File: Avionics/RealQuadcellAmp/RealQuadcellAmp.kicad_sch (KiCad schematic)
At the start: 45 parts, among them U1 OPA1642AID, U2 OPA1642AID, U3 OPA1642AID, U4 OPA1642AID

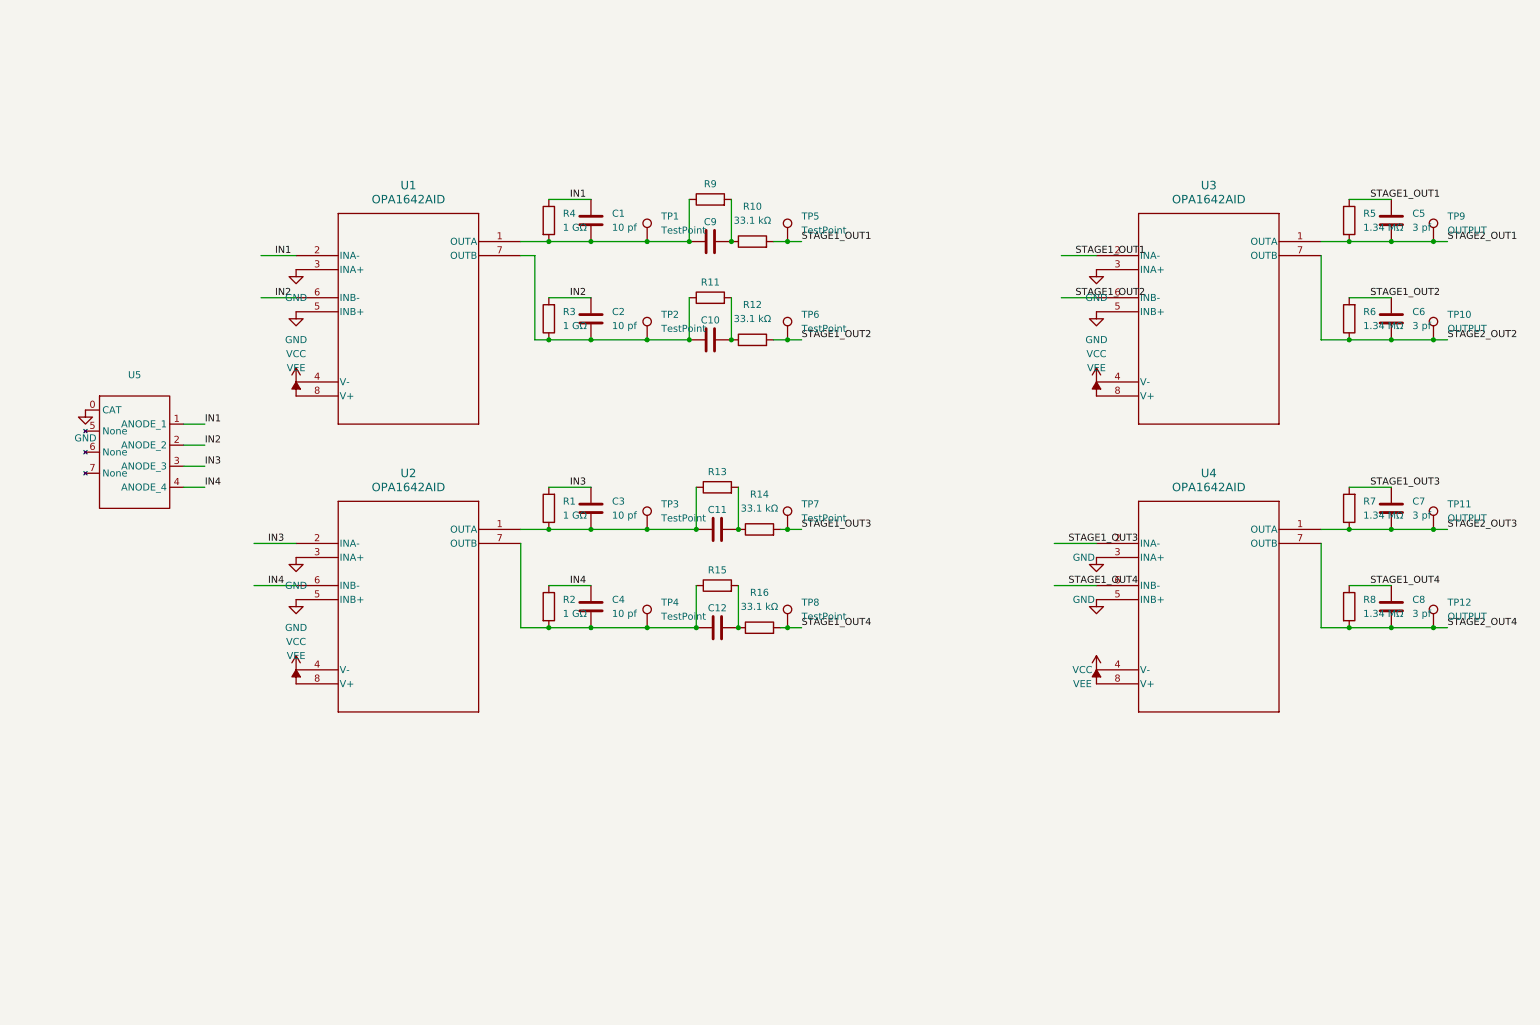
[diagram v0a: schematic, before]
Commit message: added voltage divider and adjusted routing of quadcell
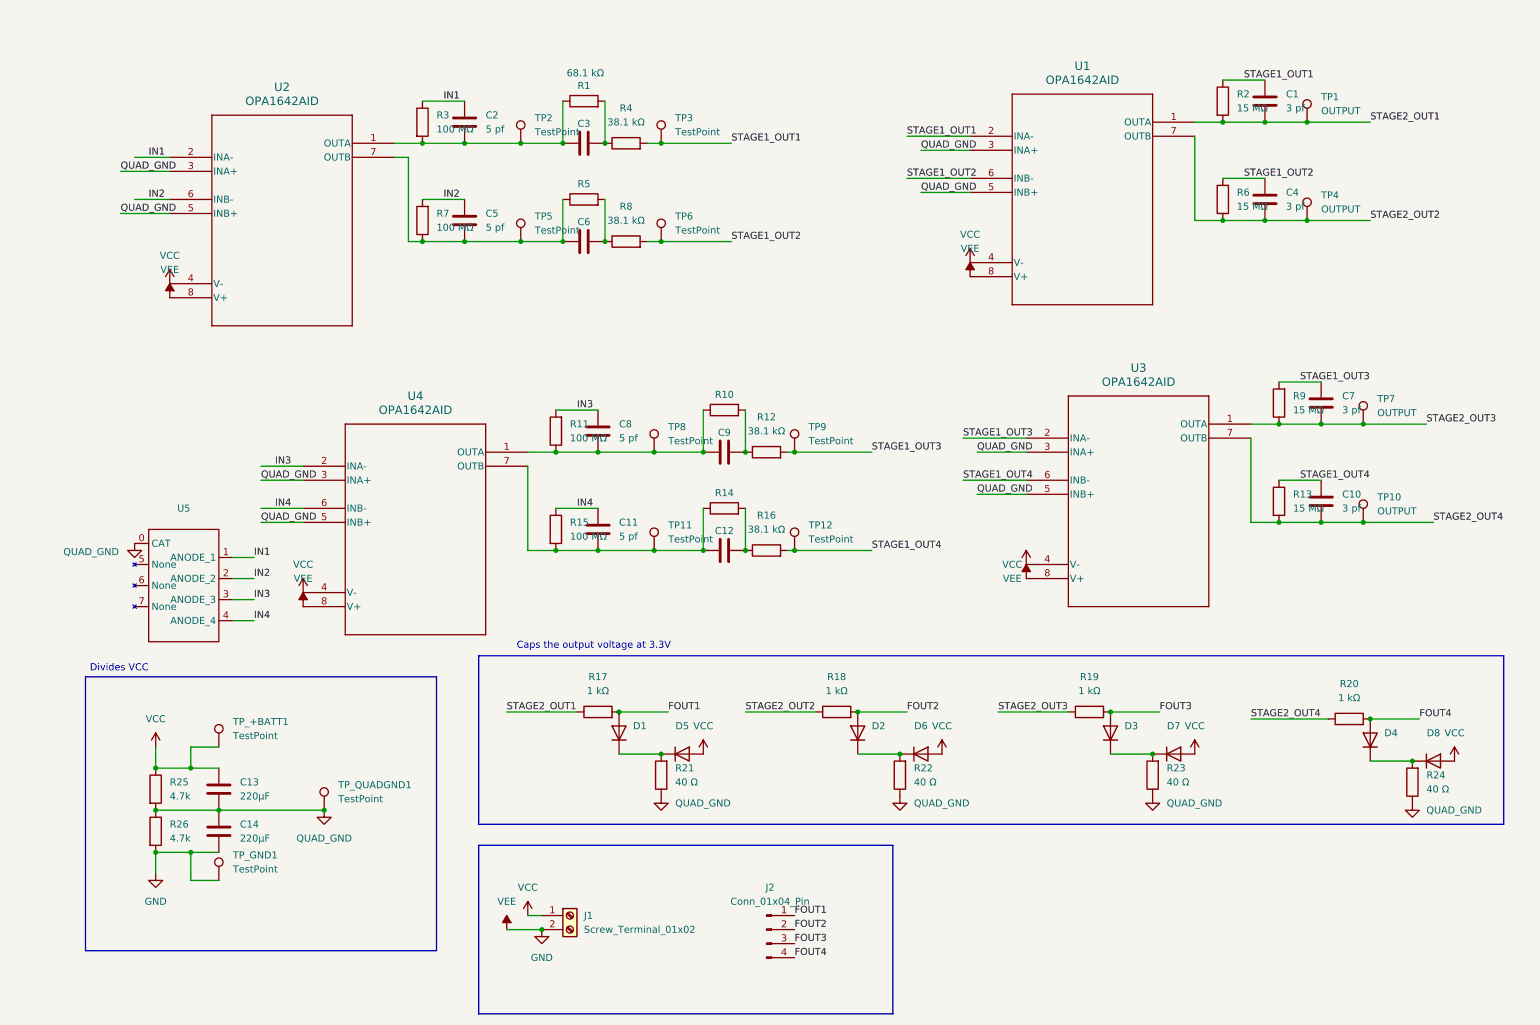
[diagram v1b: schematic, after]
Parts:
- added C13, C14: 220µF, Capacitor_SMD:C_0805_2012Metric_Pad1.18x1.45mm_HandSolder, symbol Device:C
- added D1, D2, D3, D4, D5, D6, D7, D8: ~, Diode_SMD:D_0805_2012Metric_Pad1.15x1.40mm_HandSolder, symbol Diode:1N4001
- added J1: Screw_Terminal_01x02, TerminalBlock:TerminalBlock_bornier-2_P5.08mm, symbol Connector:Screw_Terminal_01x02
- added J2: Conn_01x04_Pin, Connector_PinHeader_2.54mm:PinHeader_1x04_P2.54mm_Vertical, symbol Connector:Conn_01x04_Pin
- added R17, R18, R19, R20: 1 kΩ, Resistor_SMD:R_0805_2012Metric_Pad1.20x1.40mm_HandSolder, symbol Device:R
- added R21, R22, R23, R24: 40 Ω, Resistor_SMD:R_0805_2012Metric_Pad1.20x1.40mm_HandSolder, symbol Device:R
- added R25, R26: 4.7k, Resistor_SMD:R_0805_2012Metric_Pad1.20x1.40mm_HandSolder, symbol Device:R
- added TP_+BATT1, TP_GND1, TP_QUADGND1: TestPoint, TestPoint:TestPoint_THTPad_1.0x1.0mm_Drill0.5mm, symbol Connector:TestPoint
- C1: renamed from C5; footprint Capacitor_SMD:C_0603_1608Metric_Pad1.08x0.95mm_HandSolder -> Capacitor_SMD:C_0805_2012Metric_Pad1.18x1.45mm_HandSolder
- C10: renamed from C8; footprint Capacitor_SMD:C_0603_1608Metric_Pad1.08x0.95mm_HandSolder -> Capacitor_SMD:C_0805_2012Metric_Pad1.18x1.45mm_HandSolder
- C11: renamed from C4; value 10 pf -> 5 pf; footprint Capacitor_SMD:C_0603_1608Metric_Pad1.08x0.95mm_HandSolder -> Capacitor_SMD:C_0805_2012Metric_Pad1.18x1.45mm_HandSolder
- C12, C7: footprint Capacitor_SMD:C_0603_1608Metric_Pad1.08x0.95mm_HandSolder -> Capacitor_SMD:C_0805_2012Metric_Pad1.18x1.45mm_HandSolder
- C2: renamed from C1; value 10 pf -> 5 pf; footprint Capacitor_SMD:C_0603_1608Metric_Pad1.08x0.95mm_HandSolder -> Capacitor_SMD:C_0805_2012Metric_Pad1.18x1.45mm_HandSolder
- C3: renamed from C9; footprint Capacitor_SMD:C_0603_1608Metric_Pad1.08x0.95mm_HandSolder -> Capacitor_SMD:C_0805_2012Metric_Pad1.18x1.45mm_HandSolder
- C4: renamed from C6; footprint Capacitor_SMD:C_0603_1608Metric_Pad1.08x0.95mm_HandSolder -> Capacitor_SMD:C_0805_2012Metric_Pad1.18x1.45mm_HandSolder
- C5: renamed from C2; value 10 pf -> 5 pf; footprint Capacitor_SMD:C_0603_1608Metric_Pad1.08x0.95mm_HandSolder -> Capacitor_SMD:C_0805_2012Metric_Pad1.18x1.45mm_HandSolder
- C6: renamed from C10; footprint Capacitor_SMD:C_0603_1608Metric_Pad1.08x0.95mm_HandSolder -> Capacitor_SMD:C_0805_2012Metric_Pad1.18x1.45mm_HandSolder
- C8: renamed from C3; value 10 pf -> 5 pf; footprint Capacitor_SMD:C_0603_1608Metric_Pad1.08x0.95mm_HandSolder -> Capacitor_SMD:C_0805_2012Metric_Pad1.18x1.45mm_HandSolder
- C9: renamed from C11; footprint Capacitor_SMD:C_0603_1608Metric_Pad1.08x0.95mm_HandSolder -> Capacitor_SMD:C_0805_2012Metric_Pad1.18x1.45mm_HandSolder
- R1: renamed from R9; value 0.1 MΩ -> 68.1 kΩ; footprint Resistor_SMD:R_0603_1608Metric_Pad0.98x0.95mm_HandSolder -> Resistor_SMD:R_0805_2012Metric_Pad1.20x1.40mm_HandSolder
- R10: renamed from R13; value 0.1 MΩ -> 68.1 kΩ; footprint Resistor_SMD:R_0603_1608Metric_Pad0.98x0.95mm_HandSolder -> Resistor_SMD:R_0805_2012Metric_Pad1.20x1.40mm_HandSolder
- R11: renamed from R1; value 1 GΩ -> 100 MΩ; footprint Resistor_SMD:R_1206_3216Metric_Pad1.30x1.75mm_HandSolder -> Resistor_SMD:R_0805_2012Metric_Pad1.20x1.40mm_HandSolder
- R12: renamed from R14; value 33.1 kΩ -> 38.1 kΩ; footprint Resistor_SMD:R_0603_1608Metric_Pad0.98x0.95mm_HandSolder -> Resistor_SMD:R_0805_2012Metric_Pad1.20x1.40mm_HandSolder
- R13: renamed from R8; value 1.34 MΩ -> 15 MΩ; footprint Resistor_SMD:R_0603_1608Metric_Pad0.98x0.95mm_HandSolder -> Resistor_SMD:R_0805_2012Metric_Pad1.20x1.40mm_HandSolder
- R14: renamed from R15; value 0.1 MΩ -> 68.1 kΩ; footprint Resistor_SMD:R_0603_1608Metric_Pad0.98x0.95mm_HandSolder -> Resistor_SMD:R_0805_2012Metric_Pad1.20x1.40mm_HandSolder
- R15: renamed from R2; value 1 GΩ -> 100 MΩ; footprint Resistor_SMD:R_1206_3216Metric_Pad1.30x1.75mm_HandSolder -> Resistor_SMD:R_0805_2012Metric_Pad1.20x1.40mm_HandSolder
- R16: value 33.1 kΩ -> 38.1 kΩ; footprint Resistor_SMD:R_0603_1608Metric_Pad0.98x0.95mm_HandSolder -> Resistor_SMD:R_0805_2012Metric_Pad1.20x1.40mm_HandSolder
- R2: renamed from R5; value 1.34 MΩ -> 15 MΩ; footprint Resistor_SMD:R_0603_1608Metric_Pad0.98x0.95mm_HandSolder -> Resistor_SMD:R_0805_2012Metric_Pad1.20x1.40mm_HandSolder
- R3: renamed from R4; value 1 GΩ -> 100 MΩ; footprint Resistor_SMD:R_1206_3216Metric_Pad1.30x1.75mm_HandSolder -> Resistor_SMD:R_0805_2012Metric_Pad1.20x1.40mm_HandSolder
- R4: renamed from R10; value 33.1 kΩ -> 38.1 kΩ; footprint Resistor_SMD:R_0603_1608Metric_Pad0.98x0.95mm_HandSolder -> Resistor_SMD:R_0805_2012Metric_Pad1.20x1.40mm_HandSolder
- R5: renamed from R11; value 0.1 MΩ -> 68.1 kΩ; footprint Resistor_SMD:R_0603_1608Metric_Pad0.98x0.95mm_HandSolder -> Resistor_SMD:R_0805_2012Metric_Pad1.20x1.40mm_HandSolder
- R6: value 1.34 MΩ -> 15 MΩ; footprint Resistor_SMD:R_0603_1608Metric_Pad0.98x0.95mm_HandSolder -> Resistor_SMD:R_0805_2012Metric_Pad1.20x1.40mm_HandSolder
- R7: renamed from R3; value 1 GΩ -> 100 MΩ; footprint Resistor_SMD:R_1206_3216Metric_Pad1.30x1.75mm_HandSolder -> Resistor_SMD:R_0805_2012Metric_Pad1.20x1.40mm_HandSolder
- R8: renamed from R12; value 33.1 kΩ -> 38.1 kΩ; footprint Resistor_SMD:R_0603_1608Metric_Pad0.98x0.95mm_HandSolder -> Resistor_SMD:R_0805_2012Metric_Pad1.20x1.40mm_HandSolder
- R9: renamed from R7; value 1.34 MΩ -> 15 MΩ; footprint Resistor_SMD:R_0603_1608Metric_Pad0.98x0.95mm_HandSolder -> Resistor_SMD:R_0805_2012Metric_Pad1.20x1.40mm_HandSolder
- renumbered TP9 to TP1, TP12 to TP10, TP4 to TP11, TP8 to TP12, TP1 to TP2, TP5 to TP3, TP10 to TP4, TP2 to TP5, TP11 to TP7, TP3 to TP8, TP7 to TP9, U3 to U1, U1 to U2, U4 to U3, U2 to U4
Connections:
- net VEE is gone; now on net GND: U1.8 (V+), U2.8 (V+), U3.8 (V+), U4.8 (V+)
- net GND: now also C14.2, J1.2 (Pin_2), R26.2, TP_GND1.1; no longer U1.3 (INA+), U1.5 (INB+), U2.3 (INA+), U2.5 (INB+), U3.3 (INA+), U3.5 (INB+), U4.3 (INA+), U4.5 (INB+), U5.0 (CAT)
- net STAGE2_OUT1: now also R17.1
- net STAGE2_OUT2: now also R18.1
- net STAGE2_OUT3: now also R19.1
- net STAGE2_OUT4: now also R20.1
- net VCC: now also C13.1, D5.2 (A), D6.2 (A), D7.2 (A), D8.2 (A), J1.1 (Pin_1), R25.1, TP_+BATT1.1
- new net: D4.1 (K), D8.1 (K), R24.2
- new net: D1.1 (K), D5.1 (K), R21.2
- new net: D3.1 (K), D7.1 (K), R23.2
- new net: D2.1 (K), D6.1 (K), R22.2
- new net FOUT1: D1.2 (A), J2.1 (Pin_1), R17.2
- new net FOUT2: D2.2 (A), J2.2 (Pin_2), R18.2
- new net FOUT3: D3.2 (A), J2.3 (Pin_3), R19.2
- new net FOUT4: D4.2 (A), J2.4 (Pin_4), R20.2
- new net QUAD_GND: C13.2, C14.1, R21.1, R22.1, R23.1, R24.1, R25.2, R26.1, TP_QUADGND1.1, U1.3 (INA+), U1.5 (INB+), U2.3 (INA+), U2.5 (INB+), U3.3 (INA+), U3.5 (INB+), U4.3 (INA+), U4.5 (INB+), U5.0 (CAT)
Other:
- note added: "Caps the output voltage at 3.3V"
- note added: "Divides VCC"
- moved on the sheet: C1, C10, C11, C12, C2, C3, C4, C5, C6, C7, C8, C9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

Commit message: a few more small tweaks to quadcell
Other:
- moved on the sheet: C11, C12, C8, C9, R10, R11, R12, R14, R15, R16, TP11, TP12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

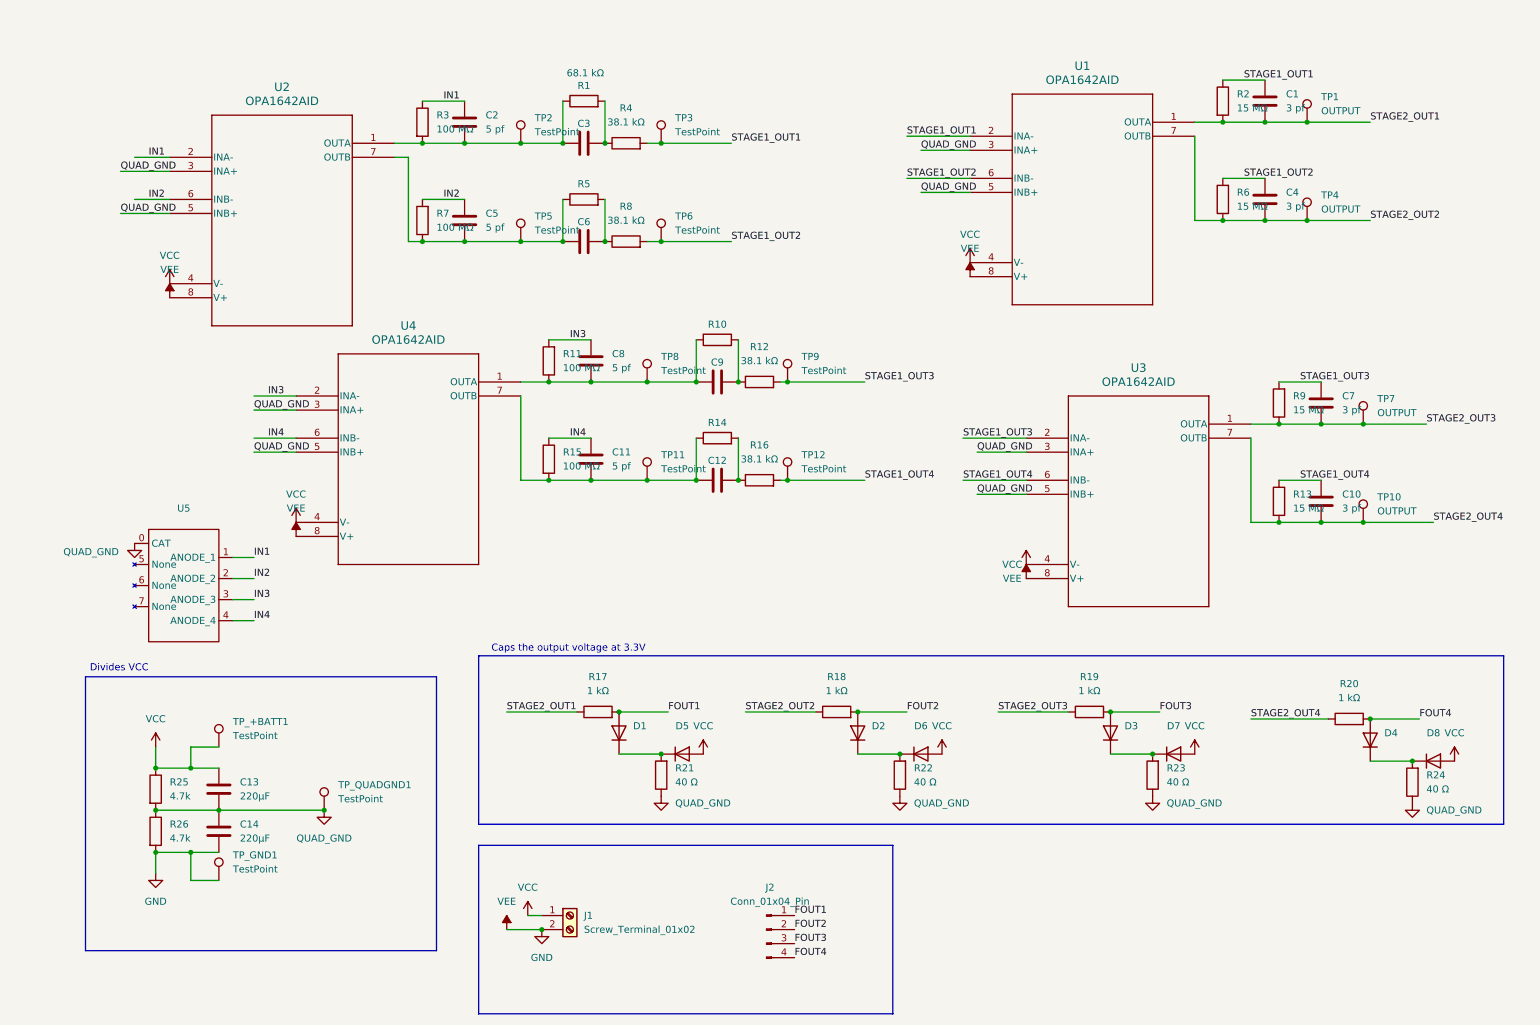
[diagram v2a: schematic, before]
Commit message: added voltage divider to quadcell
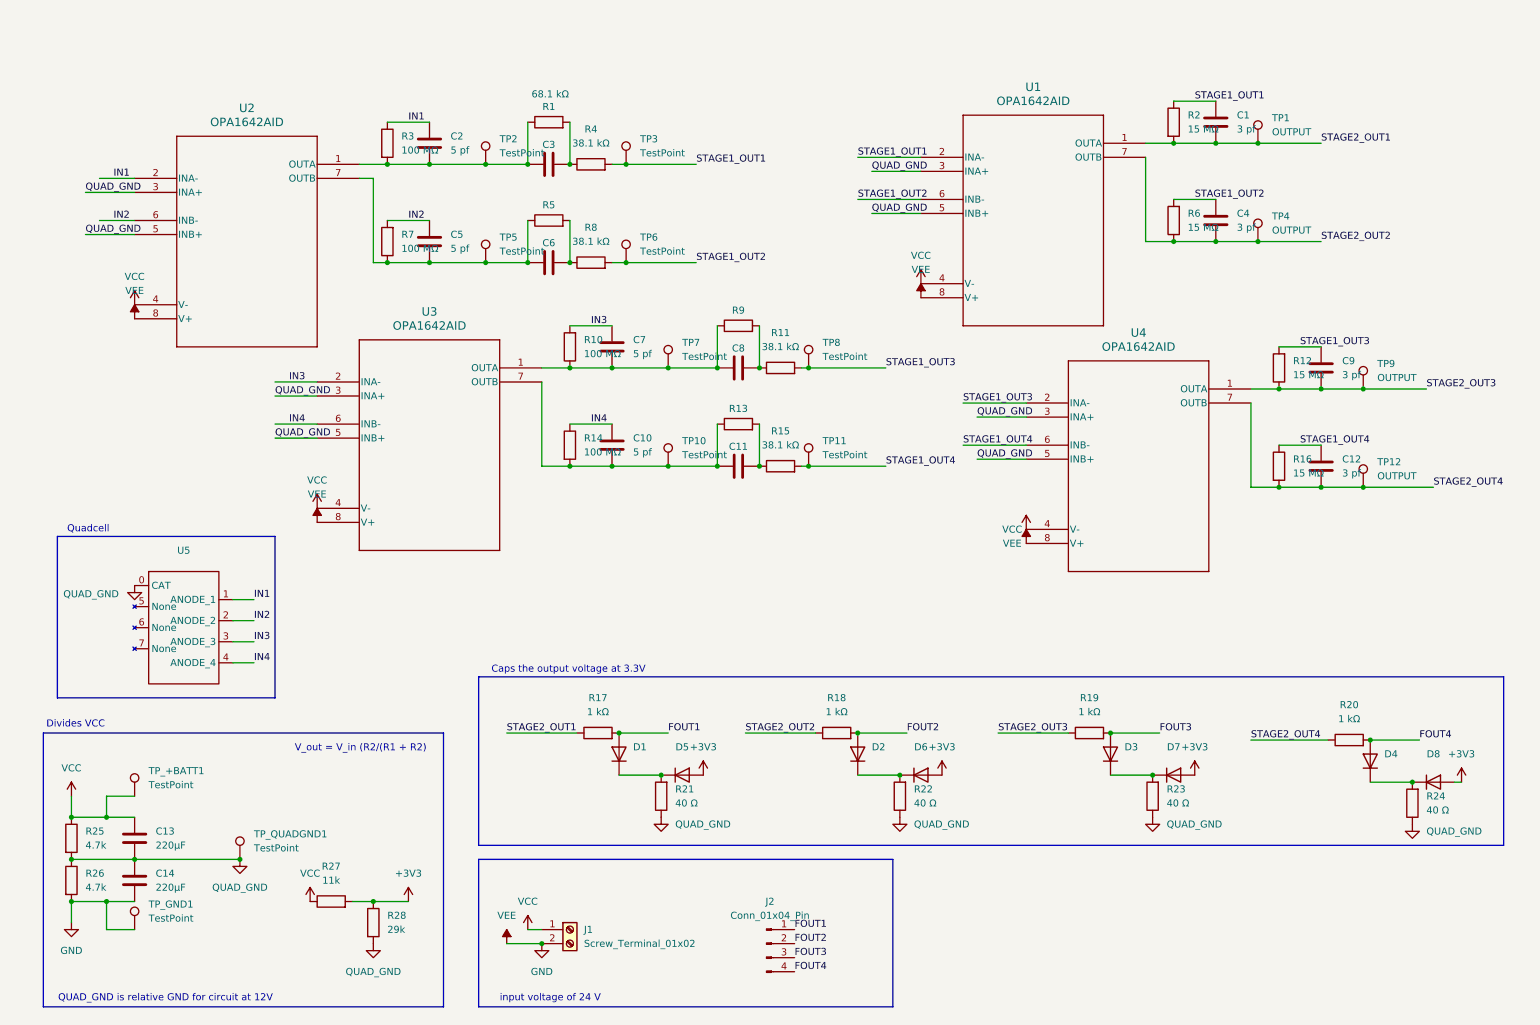
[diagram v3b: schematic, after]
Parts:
- added R27: 11k, Resistor_SMD:R_0805_2012Metric_Pad1.20x1.40mm_HandSolder, symbol Device:R
- added R28: 29k, Resistor_SMD:R_0805_2012Metric_Pad1.20x1.40mm_HandSolder, symbol Device:R
- renumbered C11 to C10, C12 to C11, C10 to C12, C8 to C7, C9 to C8, C7 to C9, R11 to R10, R12 to R11, R9 to R12, R14 to R13, R15 to R14, R16 to R15, R13 to R16, R10 to R9, TP11 to TP10, TP12 to TP11, TP10 to TP12, TP8 to TP7, TP9 to TP8, TP7 to TP9, U4 to U3, U3 to U4
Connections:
- net QUAD_GND: now also R28.2
- net VCC: now also R27.1; no longer D5.2 (A), D6.2 (A), D7.2 (A), D8.2 (A)
- new net +3V3: D5.2 (A), D6.2 (A), D7.2 (A), D8.2 (A), R27.2, R28.1
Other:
- note added: "QUAD_GND is relative GND for circuit at 12V"
- note added: "Quadcell"
- note added: "V_out = V_in (R2/(R1 + R2)"
- note added: "input voltage of 24 V"
- moved on the sheet: C1, C10, C11, C12, C13, C14, C2, C3, C4, C5, C6, C7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

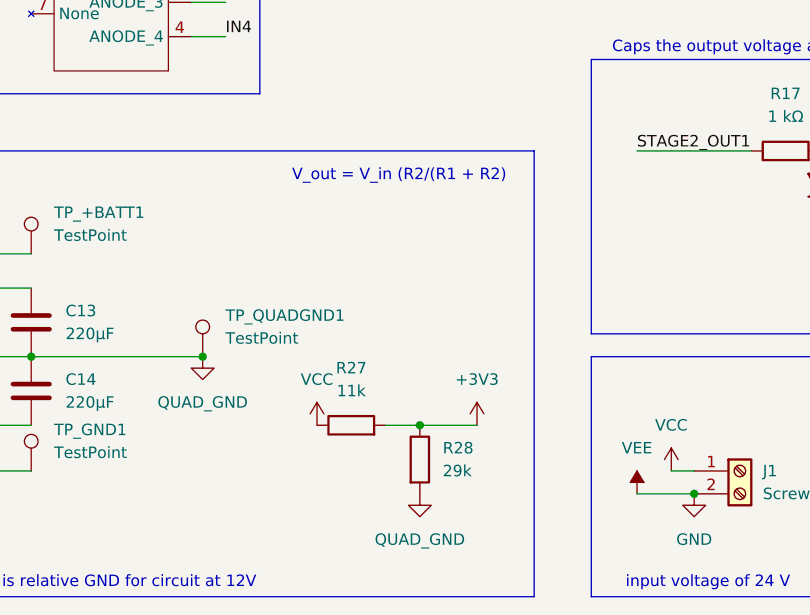
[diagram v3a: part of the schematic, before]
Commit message: added voltage regulator
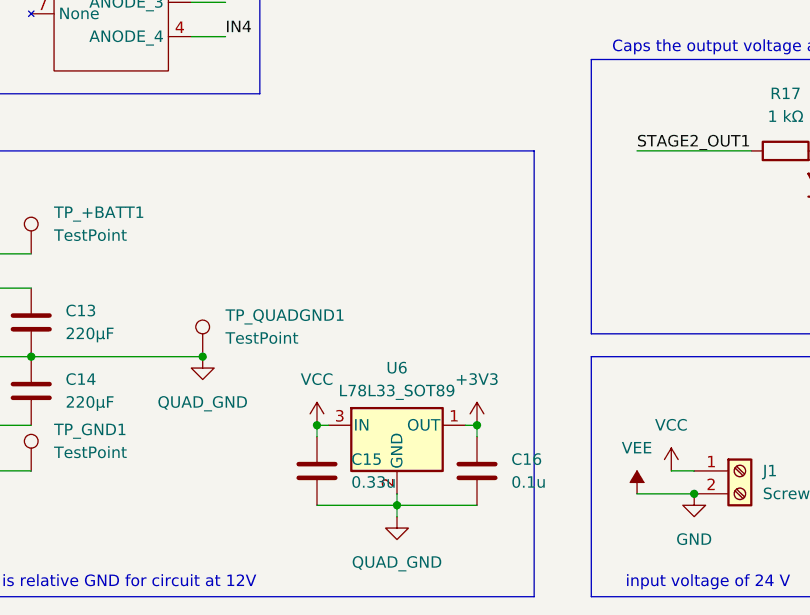
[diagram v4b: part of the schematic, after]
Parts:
- removed R27: 11k, Resistor_SMD:R_0805_2012Metric_Pad1.20x1.40mm_HandSolder, symbol Device:R
- removed R28: 29k, Resistor_SMD:R_0805_2012Metric_Pad1.20x1.40mm_HandSolder, symbol Device:R
- added C15: 0.33u, Capacitor_SMD:C_0805_2012Metric_Pad1.18x1.45mm_HandSolder, symbol Device:C
- added C16: 0.1u, Capacitor_SMD:C_0805_2012Metric_Pad1.18x1.45mm_HandSolder, symbol Device:C
- added U6: L78L33_SOT89, Package_TO_SOT_SMD:SOT-89-3, symbol Regulator_Linear:L78L33_SOT89
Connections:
- net +3V3: now also C16.1, U6.1 (OUT)
- net QUAD_GND: now also C15.2, C16.2, U6.2 (GND)
- net VCC: now also C15.1, U6.3 (IN)
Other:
- note removed: "V_out = V_in (R2/(R1 + R2)"
